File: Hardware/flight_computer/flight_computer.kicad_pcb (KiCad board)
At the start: 4 copper layers, 80 x 100 mm, 113 parts, among them J1 Micro_USB, J2 MicroSD_molex, J3 rpi_zero_w, J4 JST_8_RA, J5 JST_GH_6_RA, J6 JST_GH_4_RA, J7 JST_GH_5_RA, J8 Conn_02x03, J9 Conn_02x03, Q2 PMOS_20V_.76A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

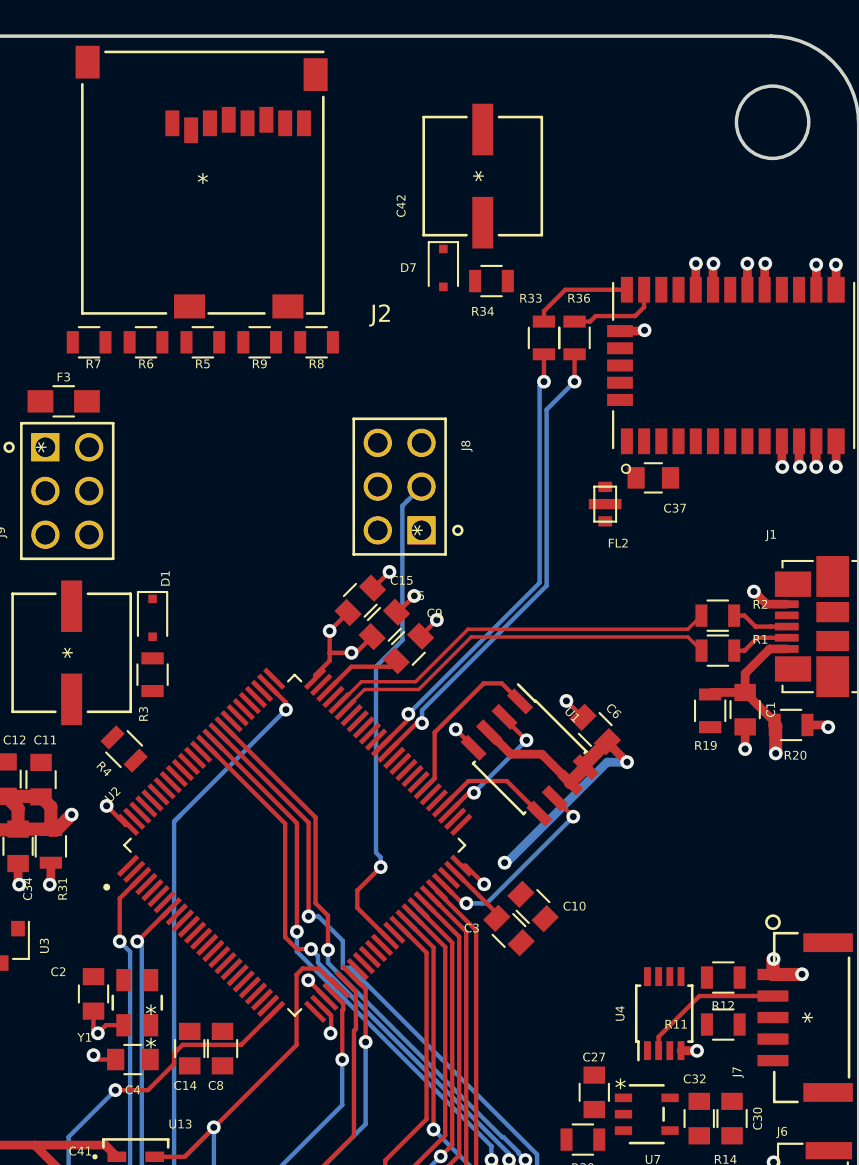
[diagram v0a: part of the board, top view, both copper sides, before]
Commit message: Wires SD card to STM
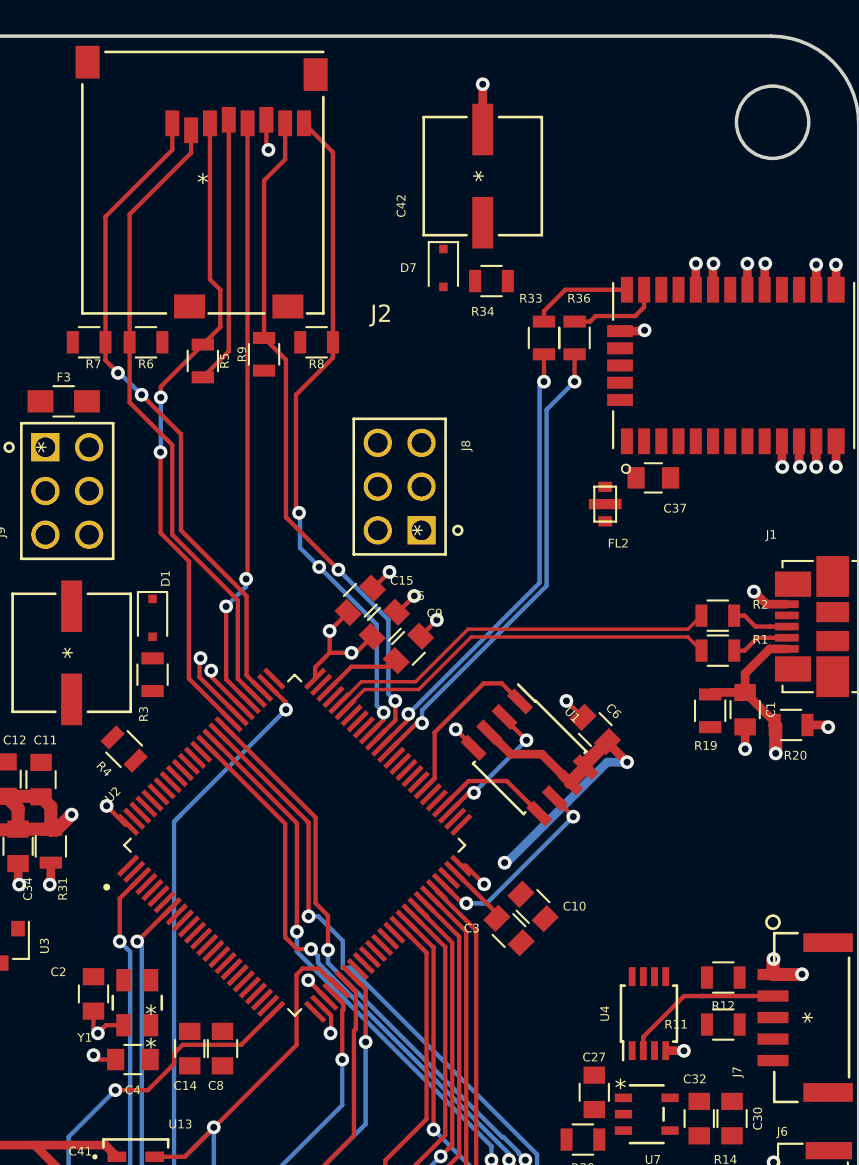
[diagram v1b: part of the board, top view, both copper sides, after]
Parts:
- moved R5 1.08 mm to (121.4, 79.3), turned to 90 degrees
- moved U4 0.89 mm to (147.3, 117.2)
- moved R9 0.74 mm to (125.0, 78.9), turned to 90 degrees
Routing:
- net /SDIO_D0: track 0.00 -> 39.9 mm, vias 0 -> 2
- net /SDIO_D1: track 0.00 -> 39.5 mm, vias 0 -> 3
- net /SDIO_D2: track 0.00 -> 38.4 mm, vias 0 -> 2
- net /SDIO_CMD: track 0.00 -> 38.1 mm, vias 0 -> 2
- net /SDIO_D3: track 0.00 -> 37.4 mm
- net /SDIO_CK: track 0.00 -> 34.8 mm, vias 0 -> 2
- net /FMU_UART7_RX: track 28.8 -> 0.00 mm, vias 1 -> 0
- net /VDD_3V3_STM: track 44.7 -> 60.2 mm
- net GND: track 173.5 -> 177.9 mm, vias 76 -> 78
- net /SERVO_CH2_GPIO: track 0.00 -> 4.26 mm, vias 0 -> 1
- net /SERVO_CH1_GPIO: track 0.00 -> 3.02 mm, vias 0 -> 1
- net /CONNECTORS/rc_in: track 8.42 -> 9.56 mm

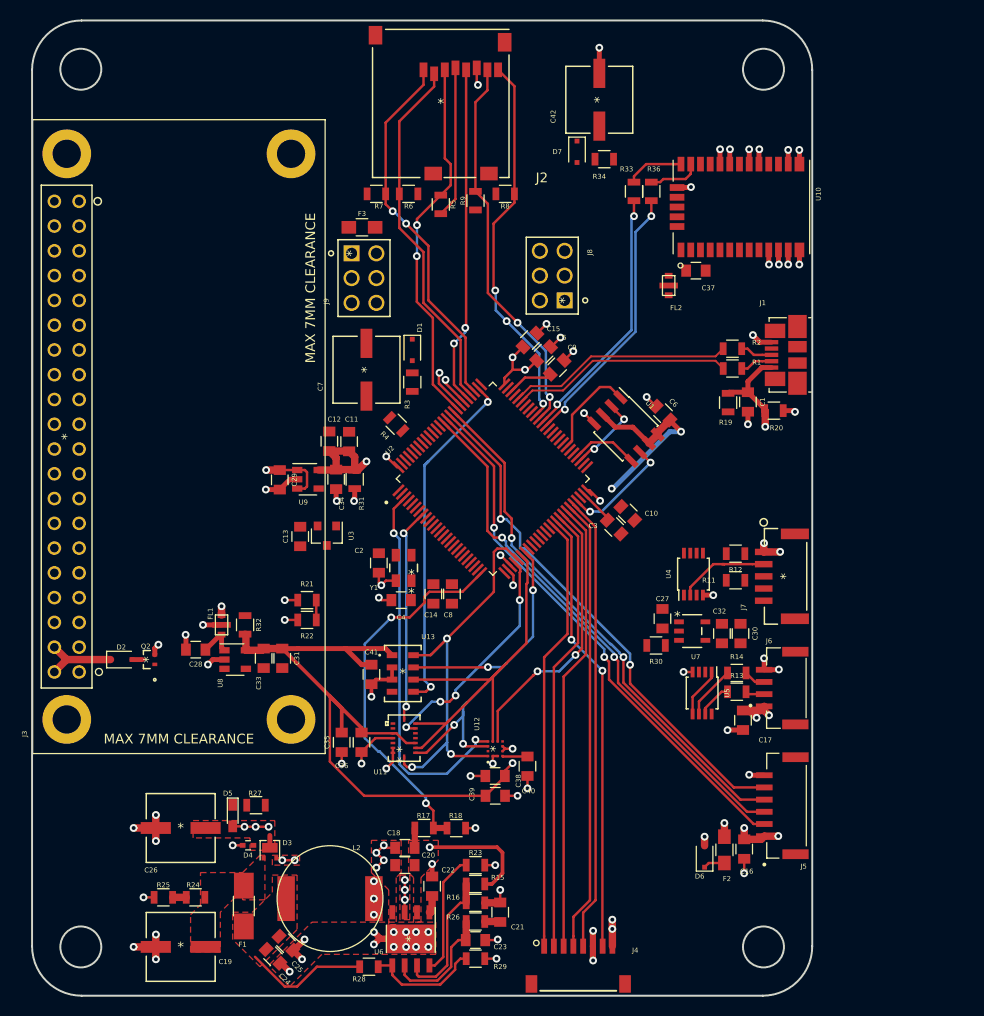
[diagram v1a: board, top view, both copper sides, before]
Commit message: Wires rpi, gps, and telem
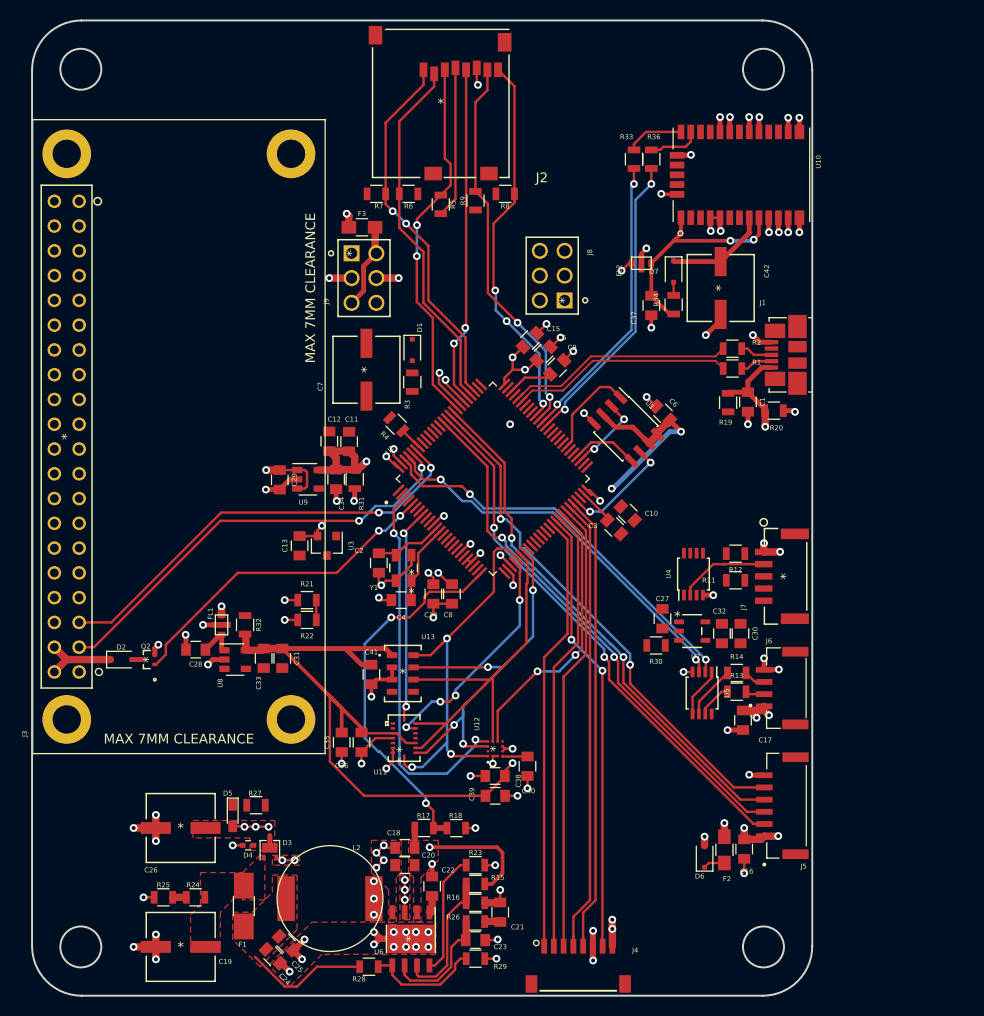
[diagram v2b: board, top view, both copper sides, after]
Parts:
- moved C42 23.0 mm to (150.1, 87.9), turned to 270 degrees
- moved R34 16.5 mm to (145.3, 89.6), turned to 270 degrees
- moved D7 15.8 mm to (145.3, 86.2)
- moved C37 5.80 mm to (143.0, 89.7), turned to 90 degrees
- moved FL2 3.61 mm to (142.0, 85.3), turned to 0 degrees
- moved U10 3.30 mm to (152.2, 76.3)
- moved R33 3.30 mm to (141.2, 74.7)
- moved R36 3.30 mm to (143.0, 74.7)
- moved U3 1.03 mm to (109.7, 114.3)
- moved C13 0.95 mm to (106.9, 114.3)
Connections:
- net /SPEKTRUM_POWER_CTRL renamed Net-(U2-Pad4)
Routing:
- net /RASPI_I2C1_SCL: track 0.00 -> 45.5 mm, vias 0 -> 2
- net /RASPI_I2C1_SDA: track 0.00 -> 45.5 mm, vias 0 -> 2
- net /FMU_USART8_RX: track 0.00 -> 41.1 mm, vias 0 -> 2
- net /FMU_USART8_TX: track 0.00 -> 41.1 mm, vias 0 -> 2
- net /BARO_CS: track 36.6 -> 0.00 mm, vias 2 -> 0
- net /RPI_POWER_CTRL: track 0.00 -> 33.8 mm, vias 0 -> 2
- net /Sensors/GPS_VCC: track 0.00 -> 23.1 mm, vias 0 -> 2
- net /VDD_3V3_SENSORS: track 73.8 -> 95.6 mm, vias 2 -> 4
- net GND: track 177.9 -> 199.5 mm, vias 78 -> 87
- net /VDD_3V3_STM: track 60.2 -> 71.4 mm, vias 8 -> 14
- net /Sensors/V_BCKP: track 0.00 -> 10.6 mm
- net /VDD_5V_AUX: track 0.00 -> 8.85 mm
- net Net-(C4-Pad2): track 0.00 -> 8.24 mm
- net Net-(C2-Pad1): track 0.00 -> 7.13 mm
- net /GPS_USART6_RX: track 26.6 -> 29.9 mm
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
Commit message: Completes initial v1 pcb traces
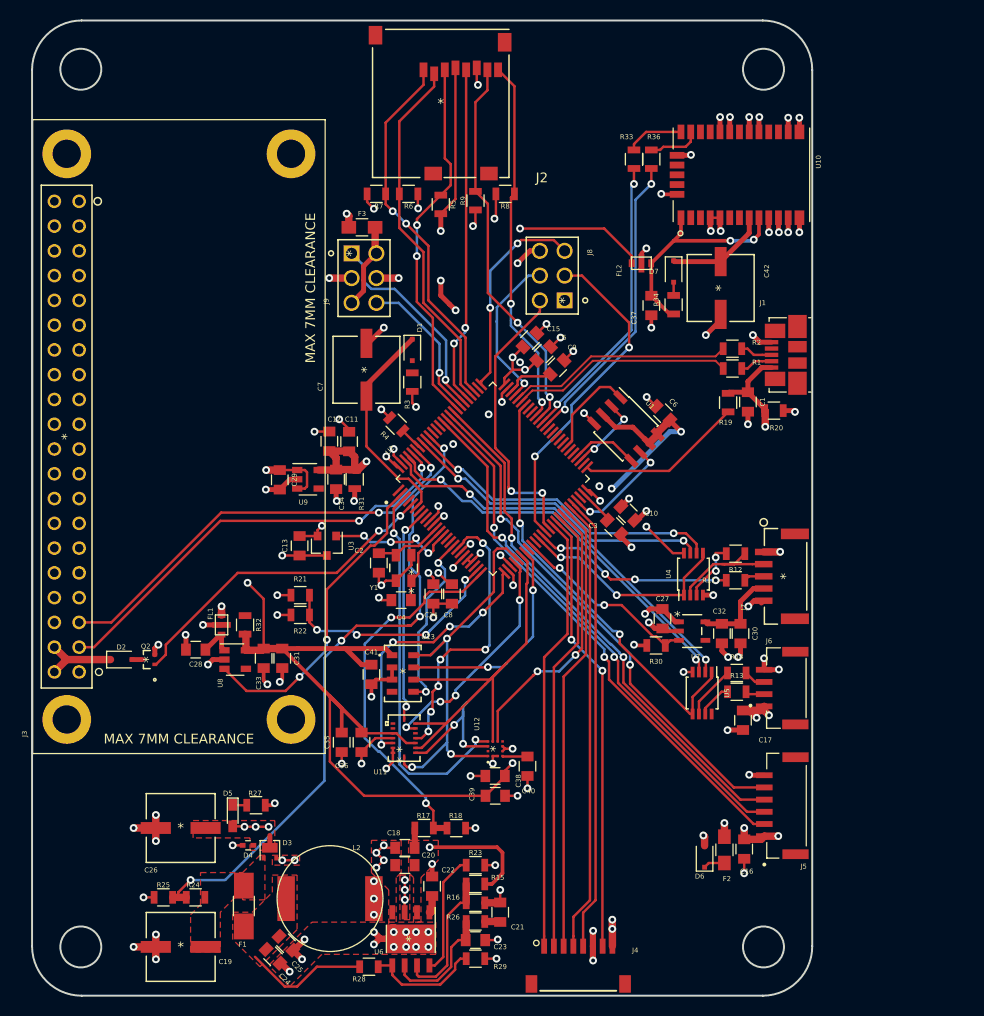
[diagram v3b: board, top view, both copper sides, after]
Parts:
- moved R21 0.86 mm to (107.0, 119.4)
- moved R22 0.86 mm to (107.0, 121.4)
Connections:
- U2 pad 15: /VDD_USB_VALID -> Net-(U2-Pad15)
- U2 pad 16: /RSSI_IN -> /DEBUG_LED_2
- U2 pad 17: Net-(U2-Pad17) -> /BARO_CS
- U2 pad 18: Net-(U2-Pad18) -> /GYRO_DRDY
- U2 pad 36: /DEBUG_LED_2 -> /SBUS_INV
- U2 pad 37: /RGB_LED -> /RSSI_IN
- U2 pad 51: Net-(U2-Pad51) -> /VDD_USB_VALID
- U2 pad 62: /GYRO_DRDY -> Net-(U2-Pad62)
- U2 pad 7: /SBUS_INV -> Net-(U2-Pad7)
- U2 pad 77: /BARO_CS -> Net-(U2-Pad77)
- U2 pad 89: Net-(U2-Pad89) -> /RGB_LED
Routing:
- net /VDD_3V3_STM: track 71.4 -> 155.4 mm, vias 14 -> 28
- net /VDD_BUCK_VALID: track 1.40 -> 67.3 mm, vias 0 -> 4
- net /VDD_3V3_SENSORS: track 95.6 -> 143.8 mm
- net /FrSky_INV: track 5.11 -> 44.7 mm, vias 0 -> 2
- net GND: track 199.5 -> 237.1 mm, vias 87 -> 106
- net /FMU_UART7_RX: track 0.00 -> 34.5 mm, vias 0 -> 2
- net /RC_OUTPUT_USART1_TX: track 0.00 -> 33.1 mm, vias 0 -> 2
- net /VDD_3V3_SENSORS_EN: track 0.00 -> 32.6 mm, vias 0 -> 2
- net /RC_INPUT_USART1_RX: track 0.00 -> 32.5 mm, vias 0 -> 2
- net /GYRO_DRDY: track 0.00 -> 29.4 mm, vias 0 -> 6
- net /FMU_UART7_TX: track 0.00 -> 29.4 mm, vias 0 -> 2
- net /IMU_GYRO_CS: track 0.00 -> 27.9 mm, vias 0 -> 4
- net /VDD_5V_SENSE: track 2.03 -> 24.4 mm, vias 0 -> 4
- net /SBUS_INV: track 0.00 -> 22.4 mm, vias 0 -> 2
- net Net-(C7-Pad1): track 0.00 -> 22.4 mm
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
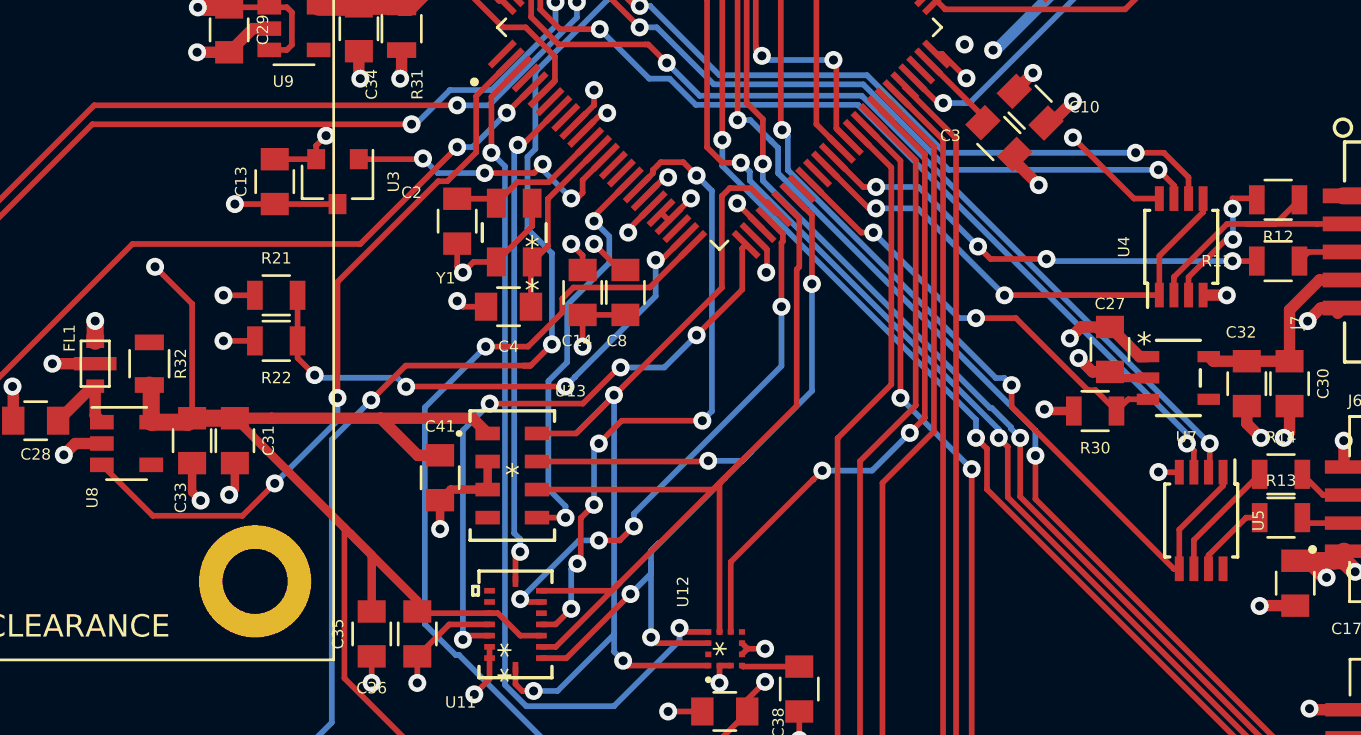
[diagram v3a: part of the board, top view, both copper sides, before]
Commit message: Adds debugging LEDs
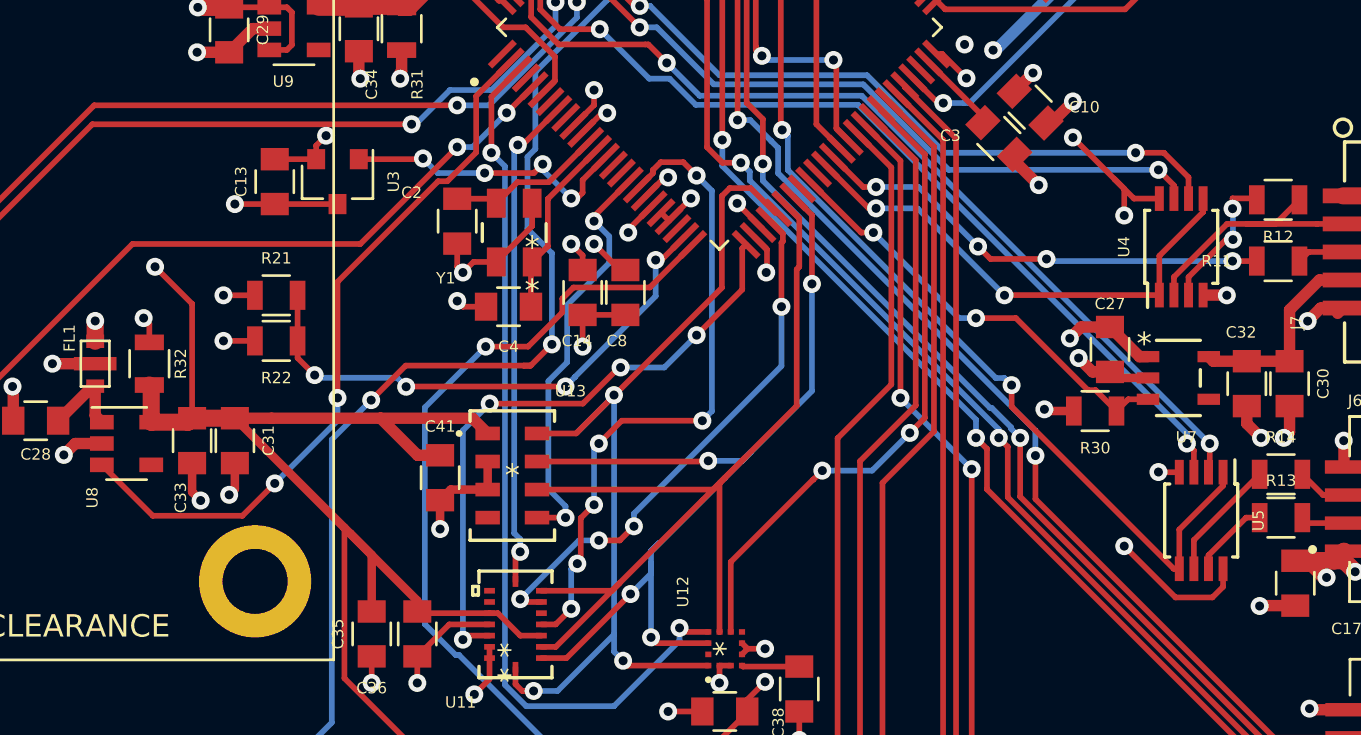
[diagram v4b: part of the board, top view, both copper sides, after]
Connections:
- net /RGB_LED renamed Net-(U2-Pad89)
- U2 pad 16: /DEBUG_LED_2 -> Net-(U2-Pad16)
- U2 pad 35: /DEBUG_LED_1 -> Net-(U2-Pad35)
- U2 pad 55: Net-(U2-Pad55) -> /DEBUG_LED_1
- U2 pad 56: Net-(U2-Pad56) -> /DEBUG_LED_2
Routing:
- net /VDD_3V3_STM: track 155.4 -> 178.2 mm, vias 28 -> 30
- net GND: track 237.1 -> 238.3 mm, vias 106 -> 107

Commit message: Adds logo to back silk
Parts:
- added G***: LOGO, drone_footprints:osprey_bitmap, B.Cu at (122.4, 103.4)
